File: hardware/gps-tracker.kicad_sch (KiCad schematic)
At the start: 95 parts, among them J1 USB_B_Micro, J2 Conn_01x07, J3 Conn_01x08, J4 Conn_01x03, J5 Conn_01x04, J6 Conn_01x03, J7 Conn_01x02, SW1 SW_Push, SW2 SW_Push, SW3 SW_Push, SW4 SW_Push, SW5 SW_Push, SW6 SW_SPDT, U1 STM32G070KBTx, U2 CH340X, U3 LTR-303ALS-01, U4 MIC5365-3.3YD5, U5 LIS2MDLTR, U6 LC86LICMD, U7 E22-900M22S, U8 TP4056, U9 MIC5365-3.3YD5

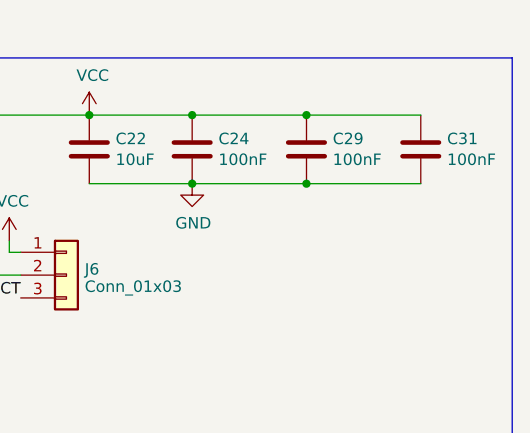
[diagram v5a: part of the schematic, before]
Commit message: Some fixes for hardware v1.0
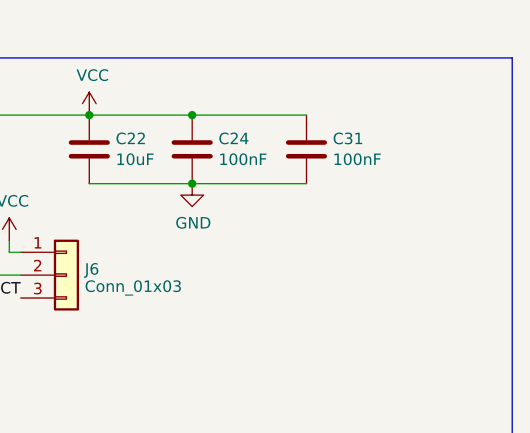
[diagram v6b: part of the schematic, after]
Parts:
- removed C29: 100nF, Capacitor_SMD:C_0402_1005Metric, symbol Device:C
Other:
- moved on the sheet: C31
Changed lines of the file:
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@@
   (junction (at 240.03 67.31) (diameter 0) (color 0 0 0 0)
   )
-  (junction (at 551.18 30.48) (diameter 0) (color 0 0 0 0)
-  )
   (junction (at 295.91 83.82) (diameter 0) (color 0 0 0 0)
   )
@@
   (junction (at 236.22 93.98) (diameter 0) (color 0 0 0 0)
   )
-  (junction (at 551.18 22.86) (diameter 0) (color 0 0 0 0)
-  )
   (junction (at 251.46 27.94) (diameter 0) (color 0 0 0 0)
   )
@@
     (stroke (width 0) (type default))
   )
-  (wire (pts (xy 551.18 22.86) (xy 563.88 22.86))
-    (stroke (width 0) (type default))
-  )
   (polyline (pts (xy 27.94 186.69) (xy 135.89 186.69))
     (stroke (width 0) (type default))
@@
     (stroke (width 0) (type default))
   )
-  (wire (pts (xy 551.18 30.48) (xy 563.88 30.48))
-    (stroke (width 0) (type default))
-  )
   (wire (pts (xy 199.39 234.95) (xy 210.82 234.95))
     (stroke (width 0) (type default))
@@
     )
   )
-  (symbol (lib_id "Device:C") (at 563.88 26.67 0) (unit 1)
+  (symbol (lib_id "Device:C") (at 551.18 26.67 0) (unit 1)
     (in_bom yes) (on_board yes) (dnp no)
-    (property "Reference" "C31" (at 566.801 25.5016 0)
+    (property "Reference" "C31" (at 554.101 25.5016 0)
       (effects (font (size 1.27 1.27)) (justify left))
     )
-    (property "Value" "100nF" (at 566.801 27.813 0)
+    (property "Value" "100nF" (at 554.101 27.813 0)
       (effects (font (size 1.27 1.27)) (justify left))
     )
-    (property "Footprint" "Capacitor_SMD:C_0402_1005Metric" (at 564.8452 30.48 0)
+    (property "Footprint" "Capacitor_SMD:C_0402_1005Metric" (at 552.1452 30.48 0)
       (effects (font (size 1.27 1.27)) hide)
     )
-    (property "Datasheet" "~" (at 563.88 26.67 0)
+    (property "Datasheet" "~" (at 551.18 26.67 0)
       (effects (font (size 1.27 1.27)) hide)
     )
-    (property "LCSC" "C307331" (at 563.88 26.67 0)
+    (property "LCSC" "C307331" (at 551.18 26.67 0)
       (effects (font (size 1.27 1.27)) hide)
     )
@@
         )
       )
-    )
-  )
-  (symbol (lib_id "Device:C") (at 551.18 26.67 0) (unit 1)
-    (in_bom yes) (on_board yes) (dnp no)
-    (property "Reference" "C29" (at 554.101 25.5016 0)
-      (effects (font (size 1.27 1.27)) (justify left))
-    )
-    (property "Value" "100nF" (at 554.101 27.813 0)
-      (effects (font (size 1.27 1.27)) (justify left))
-    )
-    (property "Footprint" "Capacitor_SMD:C_0402_1005Metric" (at 552.1452 30.48 0)
-      (effects (font (size 1.27 1.27)) hide)
-    )
-    (property "Datasheet" "~" (at 551.18 26.67 0)
-      (effects (font (size 1.27 1.27)) hide)
-    )
-    (property "LCSC" "C307331" (at 551.18 26.67 0)
-      (effects (font (size 1.27 1.27)) hide)
-    )
-    (pin "1")
-    (pin "2")
-    (instances
-      (project "gps-tracker"
-        (path "/73c7c2c3-4379-44f7-8833-283f1d18e835"
-          (reference "C29") (unit 1)
-        )
-      )
-      (project ""
-        (path "/e443e095-f4ba-4771-8554-3425f127ef3e"
-          (reference "C13") (unit 1)
-        )
-      )
